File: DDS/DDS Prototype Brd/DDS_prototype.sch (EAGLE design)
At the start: 27 parts, among them T1 ADTT1-6+, U1 AD9913, U2 S-1711A1818-I6T1U, Y1 TSX-3225 25.0000MF10P-C0

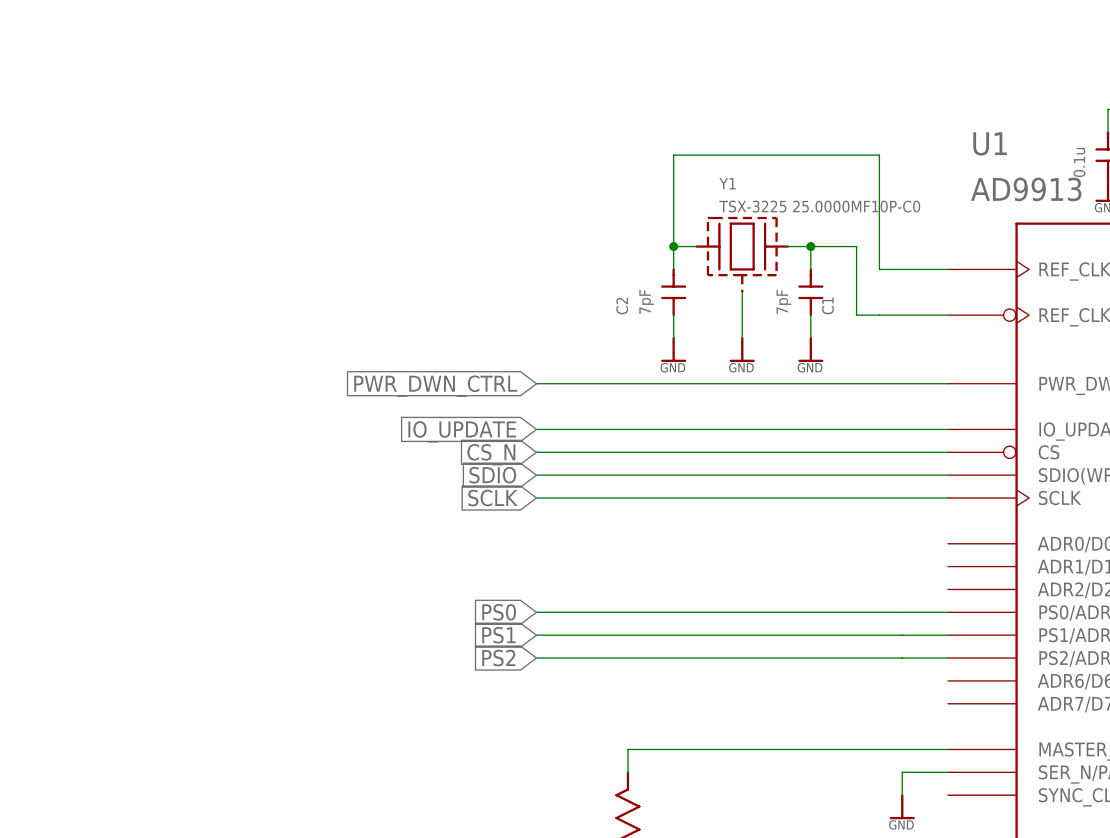
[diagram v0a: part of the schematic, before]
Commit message: added pull up/down res to ctrl lines
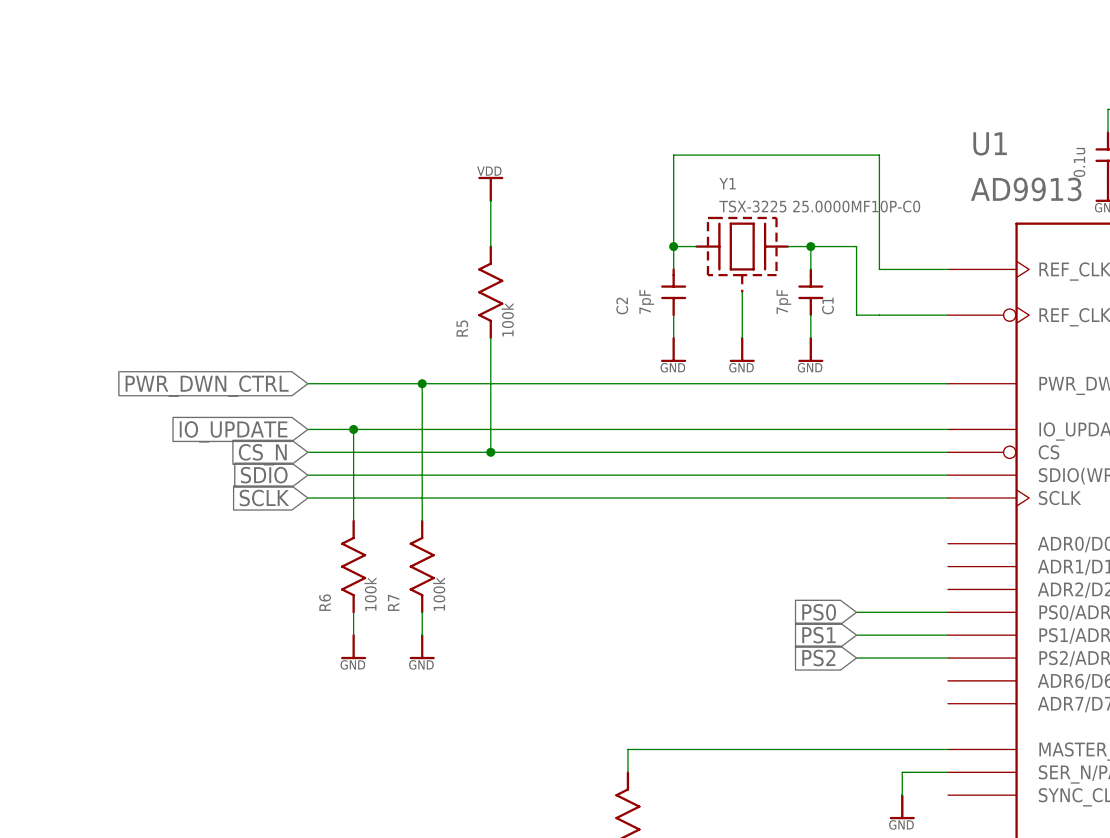
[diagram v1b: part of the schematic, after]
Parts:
- added R5, R6, R7: 100k, Resistors:RESISTOR0402
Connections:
- net N$1 renamed 3V3_PROT
- net CS_N: now also R5.P$1
- net GND: now also R6.P$1, R7.P$1
- net IO_UPDATE: now also R6.P$2
- net PWR_DWN_CTRL: now also R7.P$2
- net VDD: now also R5.P$2
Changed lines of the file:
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@@
 <?xml version="1.0" encoding="utf-8"?>
 <!DOCTYPE eagle SYSTEM "eagle.dtd">
-<eagle version="9.2.2">
+<eagle version="9.4.2">
 <drawing>
 <settings>
@@
 <part name="R1" library="Resistors" deviceset="RESISTOR" device="0402"/>
 <part name="R2" library="Resistors" deviceset="RESISTOR" device="0402"/>
+<part name="R5" library="Resistors" deviceset="RESISTOR" device="0402" value="100k"/>
+<part name="R6" library="Resistors" deviceset="RESISTOR" device="0402" value="100k"/>
+<part name="R7" library="Resistors" deviceset="RESISTOR" device="0402" value="100k"/>
+<part name="U$31" library="Supplies" deviceset="VDD" device=""/>
+<part name="U$32" library="Supplies" deviceset="GND" device=""/>
+<part name="U$33" library="Supplies" deviceset="GND" device=""/>
 </parts>
 <sheets>
@@
 <attribute name="NAME" x="165.1" y="76.2" size="1.27" layer="95" rot="R90"/>
 <attribute name="VALUE" x="170.18" y="76.2" size="1.27" layer="96" rot="R90"/>
+</instance>
+<instance part="R5" gate="G$1" x="53.34" y="132.08" smashed="yes" rot="R90">
+<attribute name="NAME" x="50.8" y="127" size="1.27" layer="95" rot="R90"/>
+<attribute name="VALUE" x="55.88" y="127" size="1.27" layer="96" rot="R90"/>
+</instance>
+<instance part="R6" gate="G$1" x="38.1" y="101.6" smashed="yes" rot="R90">
+<attribute name="NAME" x="35.56" y="96.52" size="1.27" layer="95" rot="R90"/>
+<attribute name="VALUE" x="40.64" y="96.52" size="1.27" layer="96" rot="R90"/>
+</instance>
+<instance part="R7" gate="G$1" x="45.72" y="101.6" smashed="yes" rot="R90">
+<attribute name="NAME" x="43.18" y="96.52" size="1.27" layer="95" rot="R90"/>
+<attribute name="VALUE" x="48.26" y="96.52" size="1.27" layer="96" rot="R90"/>
+</instance>
+<instance part="U$31" gate="G$1" x="53.34" y="142.24" smashed="yes">
+<attribute name="VALUE" x="53.34" y="146.05" size="1.778" layer="96" align="bottom-center"/>
+</instance>
+<instance part="U$32" gate="G$1" x="38.1" y="93.98" smashed="yes">
+<attribute name="VALUE" x="38.1" y="88.9" size="1.778" layer="96" align="bottom-center"/>
+</instance>
+<instance part="U$33" gate="G$1" x="45.72" y="93.98" smashed="yes">
+<attribute name="VALUE" x="45.72" y="88.9" size="1.778" layer="96" align="bottom-center"/>
 </instance>
 </instances>
@@
 <junction x="93.98" y="203.2"/>
 </segment>
+<segment>
+<pinref part="U$31" gate="G$1" pin="VDD"/>
+<pinref part="R5" gate="G$1" pin="P$2"/>
+<wire x1="53.34" y1="142.24" x2="53.34" y2="137.16" width="0.1524" layer="91"/>
+</segment>
 </net>
 <net name="N$9" class="0">
@@
 <wire x1="68.58" y1="22.86" x2="68.58" y2="17.78" width="0.1524" layer="91"/>
 </segment>
+<segment>
+<pinref part="R6" gate="G$1" pin="P$1"/>
+<pinref part="U$32" gate="G$1" pin="GND"/>
+<wire x1="38.1" y1="96.52" x2="38.1" y2="93.98" width="0.1524" layer="91"/>
+</segment>
+<segment>
+<pinref part="R7" gate="G$1" pin="P$1"/>
+<pinref part="U$33" gate="G$1" pin="GND"/>
+<wire x1="45.72" y1="96.52" x2="45.72" y2="93.98" width="0.1524" layer="91"/>
+</segment>
 </net>
 <net name="N$10" class="0">
@@
 <segment>
 <pinref part="U1" gate="G$1" pin="SCLK"/>
-<wire x1="104.14" y1="109.22" x2="58.42" y2="109.22" width="0.1524" layer="91"/>
-<label x="58.42" y="109.22" size="1.778" layer="95" rot="R180" xref="yes"/>
+<wire x1="104.14" y1="109.22" x2="33.02" y2="109.22" width="0.1524" layer="91"/>
+<label x="33.02" y="109.22" size="1.778" layer="95" rot="R180" xref="yes"/>
 </segment>
 <segment>
@@
 <segment>
 <pinref part="U1" gate="G$1" pin="SDIO(WR_N/RD)"/>
-<wire x1="104.14" y1="111.76" x2="58.42" y2="111.76" width="0.1524" layer="91"/>
-<label x="58.42" y="111.76" size="1.778" layer="95" rot="R180" xref="yes"/>
+<wire x1="104.14" y1="111.76" x2="33.02" y2="111.76" width="0.1524" layer="91"/>
+<label x="33.02" y="111.76" size="1.778" layer="95" rot="R180" xref="yes"/>
 </segment>
 <segment>
@@
 <segment>
 <pinref part="U1" gate="G$1" pin="CS"/>
-<wire x1="58.42" y1="114.3" x2="104.14" y2="114.3" width="0.1524" layer="91"/>
-<label x="58.42" y="114.3" size="1.778" layer="95" rot="R180" xref="yes"/>
+<wire x1="33.02" y1="114.3" x2="53.34" y2="114.3" width="0.1524" layer="91"/>
+<label x="33.02" y="114.3" size="1.778" layer="95" rot="R180" xref="yes"/>
+<pinref part="R5" gate="G$1" pin="P$1"/>
+<wire x1="53.34" y1="114.3" x2="104.14" y2="114.3" width="0.1524" layer="91"/>
+<wire x1="53.34" y1="127" x2="53.34" y2="114.3" width="0.1524" layer="91"/>
+<junction x="53.34" y="114.3"/>
 </segment>
 <segment>
@@
 <segment>
 <pinref part="U1" gate="G$1" pin="IO_UPDATE"/>
-<wire x1="104.14" y1="116.84" x2="58.42" y2="116.84" width="0.1524" layer="91"/>
-<label x="58.42" y="116.84" size="1.778" layer="95" rot="R180" xref="yes"/>
+<wire x1="104.14" y1="116.84" x2="38.1" y2="116.84" width="0.1524" layer="91"/>
+<label x="33.02" y="116.84" size="1.778" layer="95" rot="R180" xref="yes"/>
+<pinref part="R6" gate="G$1" pin="P$2"/>
+<wire x1="38.1" y1="116.84" x2="33.02" y2="116.84" width="0.1524" layer="91"/>
+<wire x1="38.1" y1="106.68" x2="38.1" y2="116.84" width="0.1524" layer="91"/>
+<junction x="38.1" y="116.84"/>
 </segment>
 <segment>
@@
 <segment>
 <pinref part="U1" gate="G$1" pin="PWR_DWN_CTRL"/>
-<wire x1="104.14" y1="121.92" x2="58.42" y2="121.92" width="0.1524" layer="91"/>
-<label x="58.42" y="121.92" size="1.778" layer="95" rot="R180" xref="yes"/>
+<wire x1="104.14" y1="121.92" x2="45.72" y2="121.92" width="0.1524" layer="91"/>
+<label x="33.02" y="121.92" size="1.778" layer="95" rot="R180" xref="yes"/>
+<pinref part="R7" gate="G$1" pin="P$2"/>
+<wire x1="45.72" y1="121.92" x2="33.02" y2="121.92" width="0.1524" layer="91"/>
+<wire x1="45.72" y1="106.68" x2="45.72" y2="121.92" width="0.1524" layer="91"/>
+<junction x="45.72" y="121.92"/>
 </segment>
 <segment>
@@
 <segment>
 <pinref part="U1" gate="G$1" pin="PS0/ADR3/D3"/>
-<wire x1="104.14" y1="96.52" x2="99.06" y2="96.52" width="0.1524" layer="91"/>
-<wire x1="99.06" y1="96.52" x2="58.42" y2="96.52" width="0.1524" layer="91"/>
-<label x="58.42" y="96.52" size="1.778" layer="95" rot="R180" xref="yes"/>
+<wire x1="104.14" y1="96.52" x2="93.98" y2="96.52" width="0.1524" layer="91"/>
+<label x="93.98" y="96.52" size="1.778" layer="95" rot="R180" xref="yes"/>
 </segment>
 <segment>
@@
 <segment>
 <pinref part="U1" gate="G$1" pin="PS1/ADR4/D4"/>
-<wire x1="104.14" y1="93.98" x2="99.06" y2="93.98" width="0.1524" layer="91"/>
-<wire x1="99.06" y1="93.98" x2="58.42" y2="93.98" width="0.1524" layer="91"/>
-<label x="58.42" y="93.98" size="1.778" layer="95" rot="R180" xref="yes"/>
+<wire x1="104.14" y1="93.98" x2="93.98" y2="93.98" width="0.1524" layer="91"/>
+<label x="93.98" y="93.98" size="1.778" layer="95" rot="R180" xref="yes"/>
 </segment>
 <segment>
@@
 <segment>
 <pinref part="U1" gate="G$1" pin="PS2/ADR5/D5"/>
-<wire x1="104.14" y1="91.44" x2="99.06" y2="91.44" width="0.1524" layer="91"/>
-<wire x1="58.42" y1="91.44" x2="99.06" y2="91.44" width="0.1524" layer="91"/>
-<label x="58.42" y="91.44" size="1.778" layer="95" rot="R180" xref="yes"/>
+<wire x1="93.98" y1="91.44" x2="104.14" y2="91.44" width="0.1524" layer="91"/>
+<label x="93.98" y="91.44" size="1.778" layer="95" rot="R180" xref="yes"/>
 </segment>
 <segment>
@@
 </segment>
 </net>
-<net name="N$1" class="0">
+<net name="3V3_PROT" class="0">
 <segment>
 <pinref part="D1" gate="G$1" pin="K"/>

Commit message: routing for pull up and pull down. not done yet.
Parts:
- removed R5: 100k, Resistors:RESISTOR0402
- added D2: (no value), Diodes:LED
- added R8: 470, Resistors:RESISTOR0402
- C9: value 0.1u -> 100p
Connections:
- net N$10 renamed RSET
- net N$9 renamed MSTR_RST
- new net N$1: D2.K, R8.P$2
- net 3V3_PROT: now also D2.A
- net CS_N: no longer R5.P$1
- net GND: now also R8.P$1
- net VDD: no longer R5.P$2
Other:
- note removed: "TODO List: make off page connectors 3.3V to 1.8V regulator 25MHz crystal passive smd libraries connector libs transformer rf connector (SMA?)"
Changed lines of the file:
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@@
 <part name="C7" library="Capacitors" deviceset="0402_CAP" device="" value="0.1u"/>
 <part name="C8" library="Capacitors" deviceset="0402_CAP" device="" value="0.1u"/>
-<part name="C9" library="Capacitors" deviceset="0402_CAP" device="" value="0.1u"/>
+<part name="C9" library="Capacitors" deviceset="0402_CAP" device="" value="100p"/>
 <part name="C10" library="Capacitors" deviceset="0402_CAP" device="" value="1u"/>
 <part name="C11" library="Capacitors" deviceset="0402_CAP" device="" value="0.1u"/>
@@
 <part name="R1" library="Resistors" deviceset="RESISTOR" device="0402"/>
 <part name="R2" library="Resistors" deviceset="RESISTOR" device="0402"/>
-<part name="R5" library="Resistors" deviceset="RESISTOR" device="0402" value="100k"/>
 <part name="R6" library="Resistors" deviceset="RESISTOR" device="0402" value="100k"/>
 <part name="R7" library="Resistors" deviceset="RESISTOR" device="0402" value="100k"/>
-<part name="U$31" library="Supplies" deviceset="VDD" device=""/>
 <part name="U$32" library="Supplies" deviceset="GND" device=""/>
 <part name="U$33" library="Supplies" deviceset="GND" device=""/>
+<part name="D2" library="Diodes" deviceset="LED" device=""/>
+<part name="R8" library="Resistors" deviceset="RESISTOR" device="0402" value="470"/>
+<part name="U$34" library="Supplies" deviceset="GND" device=""/>
 </parts>
 <sheets>
 <sheet>
 <plain>
-<text x="231.14" y="208.28" size="1.778" layer="95" align="top-left">TODO List:
-make off page connectors
-3.3V to 1.8V regulator
-25MHz crystal
-passive smd libraries
-connector libs
-transformer
-rf connector (SMA?)</text>
 </plain>
 <instances>
@@
 <attribute name="VALUE" x="170.18" y="76.2" size="1.27" layer="96" rot="R90"/>
 </instance>
-<instance part="R5" gate="G$1" x="53.34" y="132.08" smashed="yes" rot="R90">
-<attribute name="NAME" x="50.8" y="127" size="1.27" layer="95" rot="R90"/>
-<attribute name="VALUE" x="55.88" y="127" size="1.27" layer="96" rot="R90"/>
-</instance>
 <instance part="R6" gate="G$1" x="38.1" y="101.6" smashed="yes" rot="R90">
 <attribute name="NAME" x="35.56" y="96.52" size="1.27" layer="95" rot="R90"/>
@@
 <attribute name="VALUE" x="48.26" y="96.52" size="1.27" layer="96" rot="R90"/>
 </instance>
-<instance part="U$31" gate="G$1" x="53.34" y="142.24" smashed="yes">
-<attribute name="VALUE" x="53.34" y="146.05" size="1.778" layer="96" align="bottom-center"/>
-</instance>
 <instance part="U$32" gate="G$1" x="38.1" y="93.98" smashed="yes">
 <attribute name="VALUE" x="38.1" y="88.9" size="1.778" layer="96" align="bottom-center"/>
@@
 <instance part="U$33" gate="G$1" x="45.72" y="93.98" smashed="yes">
 <attribute name="VALUE" x="45.72" y="88.9" size="1.778" layer="96" align="bottom-center"/>
+</instance>
+<instance part="D2" gate="G$1" x="33.02" y="180.34" smashed="yes" rot="R270">
+<attribute name="NAME" x="34.925" y="182.88" size="1.27" layer="95" rot="R270"/>
+<attribute name="VALUE" x="29.21" y="182.88" size="1.27" layer="96" rot="R270"/>
+</instance>
+<instance part="R8" gate="G$1" x="33.02" y="170.18" smashed="yes" rot="R90">
+<attribute name="NAME" x="30.48" y="165.1" size="1.27" layer="95" rot="R90"/>
+<attribute name="VALUE" x="35.56" y="165.1" size="1.27" layer="96" rot="R90"/>
+</instance>
+<instance part="U$34" gate="G$1" x="33.02" y="162.56" smashed="yes">
+<attribute name="VALUE" x="33.02" y="157.48" size="1.778" layer="96" align="bottom-center"/>
 </instance>
 </instances>
@@
 <junction x="93.98" y="203.2"/>
 </segment>
-<segment>
-<pinref part="U$31" gate="G$1" pin="VDD"/>
-<pinref part="R5" gate="G$1" pin="P$2"/>
-<wire x1="53.34" y1="142.24" x2="53.34" y2="137.16" width="0.1524" layer="91"/>
-</segment>
-</net>
-<net name="N$9" class="0">
+</net>
+<net name="MSTR_RST" class="0">
 <segment>
 <pinref part="U1" gate="G$1" pin="MASTER_RESET"/>
@@
 <wire x1="45.72" y1="96.52" x2="45.72" y2="93.98" width="0.1524" layer="91"/>
 </segment>
-</net>
-<net name="N$10" class="0">
+<segment>
+<pinref part="R8" gate="G$1" pin="P$1"/>
+<pinref part="U$34" gate="G$1" pin="GND"/>
+<wire x1="33.02" y1="165.1" x2="33.02" y2="162.56" width="0.1524" layer="91"/>
+</segment>
+</net>
+<net name="RSET" class="0">
 <segment>
 <pinref part="U1" gate="G$1" pin="RSET"/>
@@
 <segment>
 <pinref part="U1" gate="G$1" pin="CS"/>
-<wire x1="33.02" y1="114.3" x2="53.34" y2="114.3" width="0.1524" layer="91"/>
 <label x="33.02" y="114.3" size="1.778" layer="95" rot="R180" xref="yes"/>
-<pinref part="R5" gate="G$1" pin="P$1"/>
-<wire x1="53.34" y1="114.3" x2="104.14" y2="114.3" width="0.1524" layer="91"/>
-<wire x1="53.34" y1="127" x2="53.34" y2="114.3" width="0.1524" layer="91"/>
-<junction x="53.34" y="114.3"/>
+<wire x1="33.02" y1="114.3" x2="104.14" y2="114.3" width="0.1524" layer="91"/>
 </segment>
 <segment>
@@
 <wire x1="20.32" y1="195.58" x2="20.32" y2="198.12" width="0.1524" layer="91"/>
 <junction x="20.32" y="198.12"/>
+<pinref part="D2" gate="G$1" pin="A"/>
+<wire x1="33.02" y1="187.96" x2="33.02" y2="182.88" width="0.1524" layer="91"/>
+<junction x="33.02" y="187.96"/>
+</segment>
+</net>
+<net name="N$1" class="0">
+<segment>
+<pinref part="D2" gate="G$1" pin="K"/>
+<pinref part="R8" gate="G$1" pin="P$2"/>
+<wire x1="33.02" y1="177.8" x2="33.02" y2="175.26" width="0.1524" layer="91"/>
 </segment>
 </net>
@@
 </drawing>
 <compatibility>
-<note version="6.3" minversion="6.2.2" severity="warning">
-Since Version 6.2.2 text objects can contain more than one line,
-which will not be processed correctly with this version.
-</note>
 <note version="8.2" severity="warning">
 Since Version 8.2, EAGLE supports online libraries. The ids

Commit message: final edits to prototype board. added bom.
final edits to prototype board. added bom. made 3d packages.
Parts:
- R1: value (none) -> 100k
- R2: value (none) -> 4.65k
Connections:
- net PS0: now also J1.4; no longer J1.3
- net PS1: now also J1.3; no longer J1.2
- net PS2: now also J1.2; no longer J1.1
- net SCLK: now also J1.1; no longer J1.4
